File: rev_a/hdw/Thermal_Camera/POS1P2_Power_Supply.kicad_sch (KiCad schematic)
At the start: 17 parts

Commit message: lots of schematic progress
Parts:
- C1001, C1004: renamed from C?; footprint Capacitors_SMD:C_0603 -> (none); Digi-Key PN 1276-1935-1-ND -> (none); display_footprint 0603 -> (none)
- C1002, C1003, C1005, C1006: renamed from C?; footprint Capacitors_SMD:C_0603 -> (none); Digi-Key PN 399-8153-1-ND -> (none); display_footprint 0603 -> (none)
- R1007, R1008: renamed from R?; footprint Resistors_SMD:R_0603 -> (none); Wattage 1/10W -> (none); display_footprint 0603 -> (none)
- R? (x3): footprint Resistors_SMD:R_0603 -> (none); Digi-Key PN 541-10.0KHCT-ND -> (none); Wattage 1/10W -> (none); display_footprint 0603 -> (none)
- R? (x2): footprint Resistors_SMD:R_0603 -> (none); Digi-Key PN 541-10.0HCT-ND -> (none); Wattage 1/10W -> (none); display_footprint 0603 -> (none)
- gave numbers to parts that had none: 3

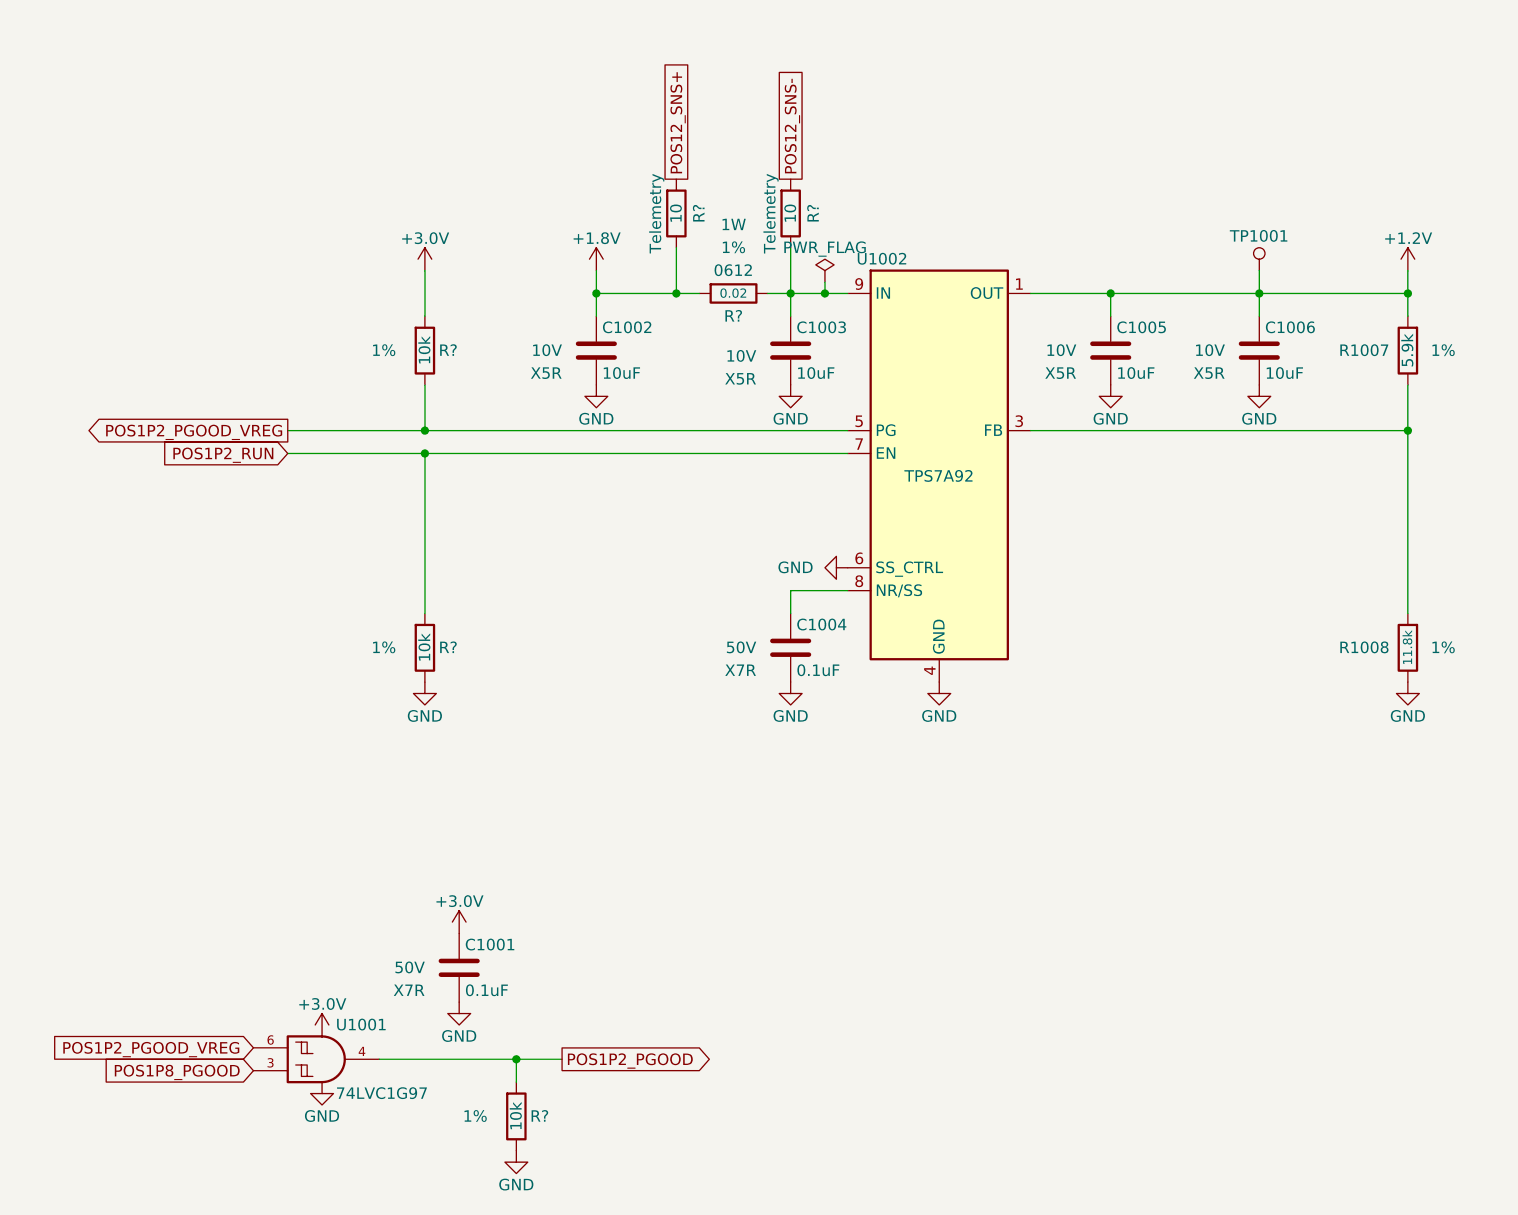
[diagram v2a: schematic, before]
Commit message: assigned a ton of footprints
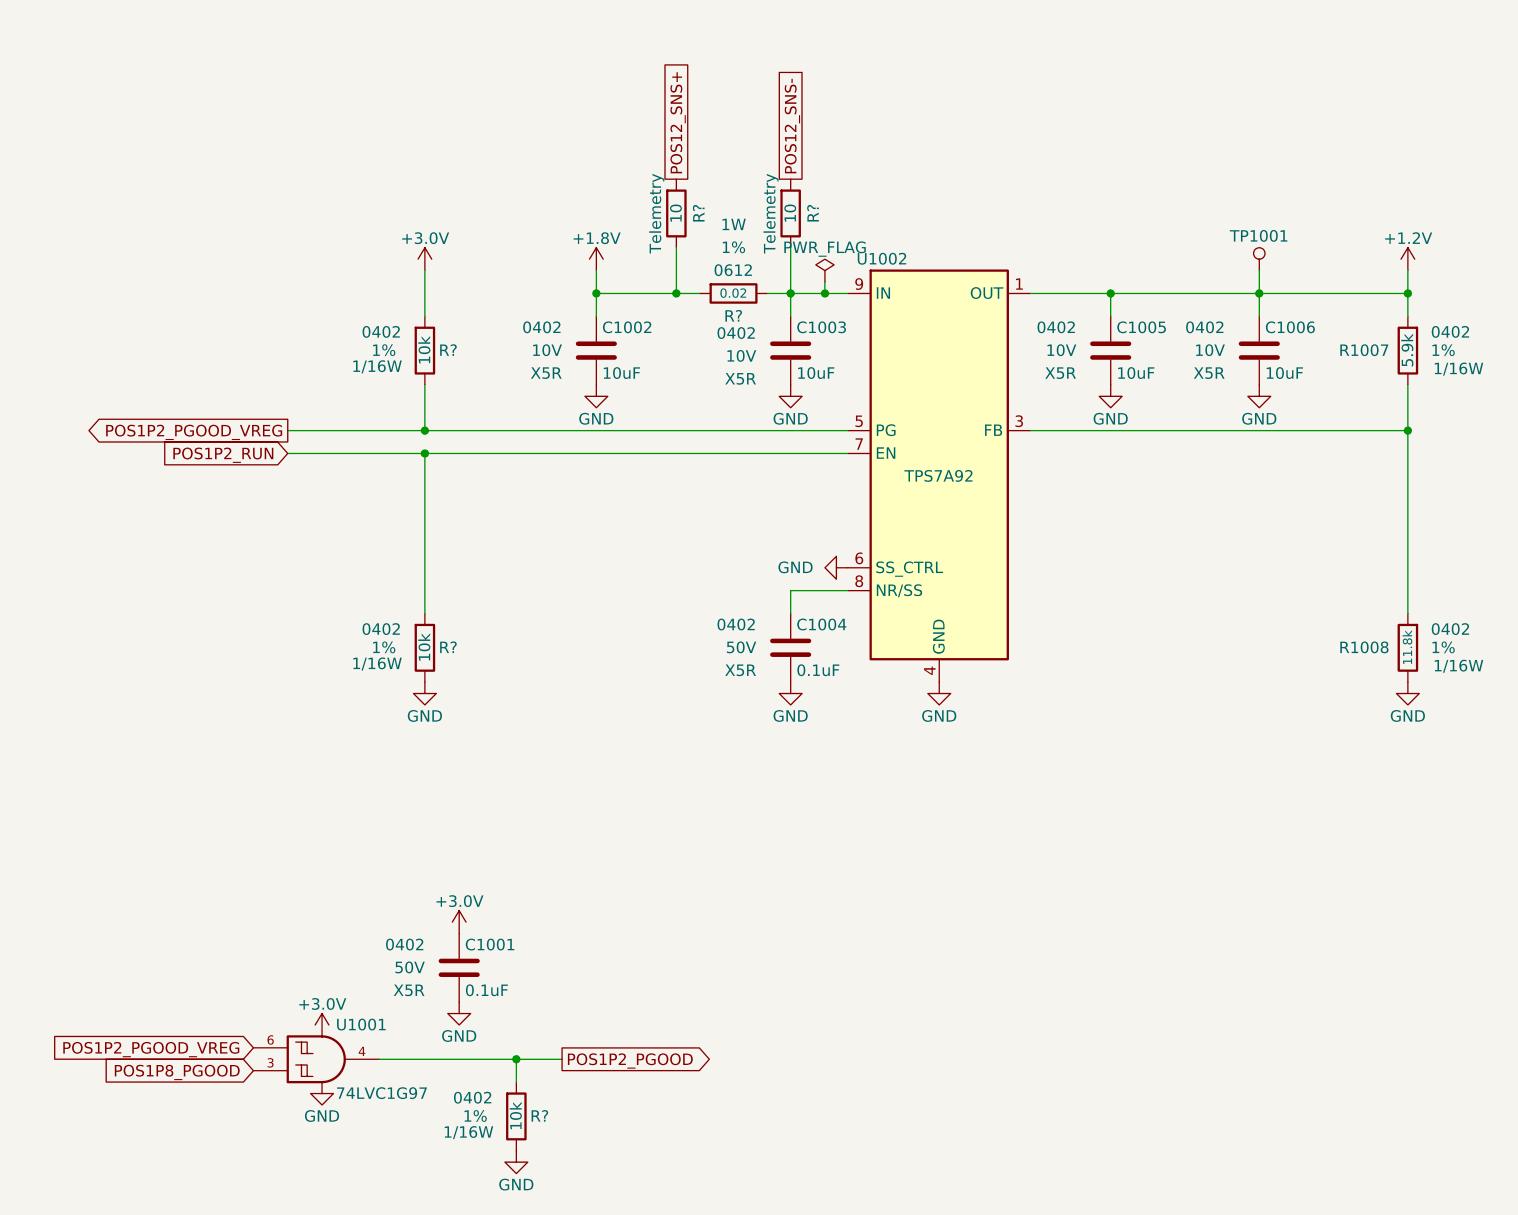
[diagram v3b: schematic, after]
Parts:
- C1001, C1004: footprint (none) -> Capacitors_SMD:C_0402; Dielectric X7R -> X5R; display_footprint (none) -> 0402
- C1002, C1003, C1005, C1006: footprint (none) -> Capacitors_SMD:C_0402; display_footprint (none) -> 0402
- R1007, R1008, R? (x5): footprint (none) -> Resistors_SMD:R_0402; Wattage (none) -> 1/16W; display_footprint (none) -> 0402
- U1001: Digi-Key PN (none) -> 296-15582-1-ND
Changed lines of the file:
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@@
 			)
 		)
-		(property "Footprint" ""
+		(property "Footprint" "Resistors_SMD:R_0402"
 			(at 88.9 165.1 0)
 			(effects
@@
 			)
 		)
-		(property "display_footprint" ""
+		(property "display_footprint" "0402"
 			(at 84.074 163.068 0)
 			(effects
@@
 			)
 		)
-		(property "Wattage" ""
+		(property "Wattage" "1/16W"
 			(at 83.566 166.878 0)
 			(effects
@@
 			)
 		)
-		(property "Footprint" ""
+		(property "Footprint" "Capacitors_SMD:C_0402"
 			(at 120.3452 83.82 0)
 			(effects
@@
 			)
 		)
-		(property "display_footprint" ""
+		(property "display_footprint" "0402"
 			(at 115.57 78.105 0)
 			(effects
@@
 			)
 		)
-		(property "Footprint" ""
+		(property "Footprint" "Capacitors_SMD:C_0402"
 			(at 120.3452 116.84 0)
 			(effects
@@
 			)
 		)
-		(property "display_footprint" ""
+		(property "display_footprint" "0402"
 			(at 115.57 110.49 0)
 			(effects
@@
 			)
 		)
-		(property "Dielectric" "X7R"
+		(property "Dielectric" "X5R"
 			(at 115.57 115.57 0)
 			(effects
@@
 			)
 		)
-		(property "Footprint" ""
+		(property "Footprint" "Resistors_SMD:R_0402"
 			(at 187.96 113.03 0)
 			(effects
@@
 			)
 		)
-		(property "display_footprint" ""
+		(property "display_footprint" "0402"
 			(at 190.5 110.998 0)
 			(effects
@@
 			)
 		)
-		(property "Wattage" ""
+		(property "Wattage" "1/16W"
 			(at 190.754 115.062 0)
 			(effects
@@
 			)
 		)
-		(property "Footprint" ""
+		(property "Footprint" "Resistors_SMD:R_0402"
 			(at 119.38 64.77 0)
 			(effects
@@
 			)
 		)
-		(property "display_footprint" ""
+		(property "display_footprint" "0402"
 			(at 116.84 64.77 90)
 			(effects
@@
 			)
 		)
-		(property "Wattage" ""
+		(property "Wattage" "1/16W"
 			(at 111.76 64.77 90)
 			(effects
@@
 			)
 		)
-		(property "Footprint" ""
+		(property "Footprint" "Resistors_SMD:R_0402"
 			(at 78.74 80.01 0)
 			(effects
@@
 			)
 		)
-		(property "display_footprint" ""
+		(property "display_footprint" "0402"
 			(at 73.914 77.978 0)
 			(effects
@@
 			)
 		)
-		(property "Wattage" ""
+		(property "Wattage" "1/16W"
 			(at 73.406 81.788 0)
 			(effects
@@
 			)
 		)
-		(property "Footprint" ""
+		(property "Footprint" "Capacitors_SMD:C_0402"
 			(at 155.9052 83.82 0)
 			(effects
@@
 			)
 		)
-		(property "display_footprint" ""
+		(property "display_footprint" "0402"
 			(at 151.13 77.47 0)
 			(effects
@@
 			)
 		)
-		(property "Footprint" ""
+		(property "Footprint" "Resistors_SMD:R_0402"
 			(at 78.74 113.03 0)
 			(effects
@@
 			)
 		)
-		(property "display_footprint" ""
+		(property "display_footprint" "0402"
 			(at 73.914 110.998 0)
 			(effects
@@
 			)
 		)
-		(property "Wattage" ""
+		(property "Wattage" "1/16W"
 			(at 73.406 114.808 0)
 			(effects
@@
 			)
 		)
-		(property "Footprint" ""
+		(property "Footprint" "Resistors_SMD:R_0402"
 			(at 187.96 80.01 0)
 			(effects
@@
 			)
 		)
-		(property "display_footprint" ""
+		(property "display_footprint" "0402"
 			(at 190.5 77.978 0)
 			(effects
@@
 			)
 		)
-		(property "Wattage" ""
+		(property "Wattage" "1/16W"
 			(at 190.754 82.042 0)
 			(effects
@@
 			)
 		)
+		(property "Digi-Key PN" "296-15582-1-ND"
+			(at 67.31 158.75 0)
+			(effects
+				(font
+					(size 1.27 1.27)
+				)
+				(hide yes)
+			)
+		)
 		(pin "1"
 		)
@@
 			)
 		)
-		(property "Footprint" ""
+		(property "Footprint" "Resistors_SMD:R_0402"
 			(at 106.68 64.77 0)
 			(effects
@@
 			)
 		)
-		(property "display_footprint" ""
+		(property "display_footprint" "0402"
 			(at 104.14 64.77 90)
 			(effects
@@
 			)
 		)
-		(property "Wattage" ""
+		(property "Wattage" "1/16W"
 			(at 99.06 64.77 90)
 			(effects
@@
 			)
 		)
-		(property "Footprint" ""
+		(property "Footprint" "Capacitors_SMD:C_0402"
 			(at 83.5152 152.4 0)
 			(effects
@@
 			)
 		)
-		(property "display_footprint" ""
+		(property "display_footprint" "0402"
 			(at 78.74 146.05 0)
 			(effects
@@
 			)
 		)
-		(property "Dielectric" "X7R"
+		(property "Dielectric" "X5R"
 			(at 78.74 151.13 0)
 			(effects
@@
 			)
 		)
-		(property "Footprint" ""
+		(property "Footprint" "Capacitors_SMD:C_0402"
 			(at 98.7552 83.82 0)
 			(effects
@@
 			)
 		)
-		(property "display_footprint" ""
+		(property "display_footprint" "0402"
 			(at 93.98 77.47 0)
 			(effects
@@
 			)
 		)
-		(property "Footprint" ""
+		(property "Footprint" "Capacitors_SMD:C_0402"
 			(at 172.4152 83.82 0)
 			(effects
@@
 			)
 		)
-		(property "display_footprint" ""
+		(property "display_footprint" "0402"
 			(at 167.64 77.47 0)
 			(effects

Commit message: assigned some part numbers
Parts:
- C1001, C1004: Digi-Key PN (none) -> 490-10697-1-ND
- C1002, C1003, C1005, C1006: Digi-Key PN (none) -> 490-GRM155R61A106ME11DCT-ND
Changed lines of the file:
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@@
 			)
 		)
-		(property "Digi-Key PN" ""
+		(property "Digi-Key PN" "490-GRM155R61A106ME11DCT-ND"
 			(at 119.38 80.01 0)
 			(effects
@@
 			)
 		)
-		(property "Digi-Key PN" ""
+		(property "Digi-Key PN" "490-10697-1-ND"
 			(at 130.175 100.33 0)
 			(effects
@@
 			)
 		)
-		(property "Digi-Key PN" ""
+		(property "Digi-Key PN" "490-GRM155R61A106ME11DCT-ND"
 			(at 154.94 80.01 0)
 			(effects
@@
 			)
 		)
-		(property "Digi-Key PN" ""
+		(property "Digi-Key PN" "490-10697-1-ND"
 			(at 93.345 135.89 0)
 			(effects
@@
 			)
 		)
-		(property "Digi-Key PN" ""
+		(property "Digi-Key PN" "490-GRM155R61A106ME11DCT-ND"
 			(at 97.79 80.01 0)
 			(effects
@@
 			)
 		)
-		(property "Digi-Key PN" ""
+		(property "Digi-Key PN" "490-GRM155R61A106ME11DCT-ND"
 			(at 171.45 80.01 0)
 			(effects

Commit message: assigned resistor part numbers
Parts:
- R1007: Digi-Key PN (none) -> RMCF0402FT5K90CT-ND
- R1008: Digi-Key PN (none) -> RMCF0402FT11K8CT-ND
- R? (x3): Digi-Key PN (none) -> RMCF0402FT10K0CT-ND
- R? (x2): Digi-Key PN (none) -> RMCF0402FT10R0CT-ND
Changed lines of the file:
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@@
 			)
 		)
-		(property "Digi-Key PN" ""
+		(property "Digi-Key PN" "RMCF0402FT10K0CT-ND"
 			(at 81.28 154.94 0)
 			(effects
@@
 			)
 		)
-		(property "Digi-Key PN" ""
+		(property "Digi-Key PN" "RMCF0402FT11K8CT-ND"
 			(at 187.96 113.03 0)
 			(effects
@@
 			)
 		)
-		(property "Digi-Key PN" ""
+		(property "Digi-Key PN" "RMCF0402FT10R0CT-ND"
 			(at 119.38 64.77 0)
 			(effects
@@
 			)
 		)
-		(property "Digi-Key PN" ""
+		(property "Digi-Key PN" "RMCF0402FT10K0CT-ND"
 			(at 71.12 69.85 0)
 			(effects
@@
 			)
 		)
-		(property "Digi-Key PN" ""
+		(property "Digi-Key PN" "RMCF0402FT10K0CT-ND"
 			(at 71.12 102.87 0)
 			(effects
@@
 			)
 		)
-		(property "Digi-Key PN" ""
+		(property "Digi-Key PN" "RMCF0402FT5K90CT-ND"
 			(at 187.96 80.01 0)
 			(effects
@@
 			)
 		)
-		(property "Digi-Key PN" ""
+		(property "Digi-Key PN" "RMCF0402FT10R0CT-ND"
 			(at 106.68 64.77 0)
 			(effects

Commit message: a ton of routing progress, power planes, ehat have you
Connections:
- net POS12_SNS+ renamed POS1P2_SNS+
- net POS12_SNS- renamed POS1P2_SNS-
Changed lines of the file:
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@@
 		)
 	)
-	(global_label "POS12_SNS+"
+	(global_label "POS1P2_SNS+"
 		(shape passive)
 		(at 106.68 60.96 90)
@@
 		)
 		(property "Intersheetrefs" "${INTERSHEET_REFS}"
-			(at 106.68 46.5676 90)
+			(at 106.68 45.2976 90)
 			(effects
 				(font
@@
 		)
 	)
-	(global_label "POS12_SNS-"
+	(global_label "POS1P2_SNS-"
 		(shape passive)
 		(at 119.38 60.96 90)
@@
 		)
 		(property "Intersheetrefs" "${INTERSHEET_REFS}"
-			(at 119.38 46.5676 90)
+			(at 119.38 45.2976 90)
 			(effects
 				(font
